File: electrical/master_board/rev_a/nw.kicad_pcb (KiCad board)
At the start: 2 copper layers, 0 parts

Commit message: Inject the PCB outlines into master/center/ne/nw/se/sw PCB's.
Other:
- board outline added: 42.2 x 39 mm
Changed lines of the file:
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@@
     (uvia_drill 0.1)
   )
+  (gr_line (start 70.00 61.00) (end 70.00 26.46) (layer Edge.Cuts) (width 0.05))
+  (gr_line (start 70.00 26.46) (end 69.99 26.33) (layer Edge.Cuts) (width 0.05))
+  (gr_line (start 69.99 26.33) (end 69.98 26.19) (layer Edge.Cuts) (width 0.05))
+  (gr_line (start 69.98 26.19) (end 69.95 26.06) (layer Edge.Cuts) (width 0.05))
+  (gr_line (start 69.95 26.06) (end 69.90 25.94) (layer Edge.Cuts) (width 0.05))
+  (gr_line (start 69.90 25.94) (end 69.85 25.81) (layer Edge.Cuts) (width 0.05))
+  (gr_line (start 69.85 25.81) (end 69.79 25.69) (layer Edge.Cuts) (width 0.05))
+  (gr_line (start 69.79 25.69) (end 69.71 25.58) (layer Edge.Cuts) (width 0.05))
+  (gr_line (start 69.71 25.58) (end 69.63 25.48) (layer Edge.Cuts) (width 0.05))
+  (gr_line (start 69.63 25.48) (end 69.54 25.38) (layer Edge.Cuts) (width 0.05))
+  (gr_line (start 69.54 25.38) (end 69.43 25.29) (layer Edge.Cuts) (width 0.05))
+  (gr_line (start 69.43 25.29) (end 69.33 25.21) (layer Edge.Cuts) (width 0.05))
+  (gr_line (start 69.33 25.21) (end 69.21 25.14) (layer Edge.Cuts) (width 0.05))
+  (gr_line (start 69.21 25.14) (end 69.09 25.08) (layer Edge.Cuts) (width 0.05))
+  (gr_line (start 69.09 25.08) (end 68.96 25.04) (layer Edge.Cuts) (width 0.05))
+  (gr_line (start 68.96 25.04) (end 68.83 25.00) (layer Edge.Cuts) (width 0.05))
+  (gr_line (start 68.83 25.00) (end 68.70 24.98) (layer Edge.Cuts) (width 0.05))
+  (gr_line (start 68.70 24.98) (end 68.57 24.96) (layer Edge.Cuts) (width 0.05))
+  (gr_line (start 68.57 24.96) (end 68.43 24.96) (layer Edge.Cuts) (width 0.05))
+  (gr_line (start 68.43 24.96) (end 68.30 24.98) (layer Edge.Cuts) (width 0.05))
+  (gr_line (start 68.30 24.98) (end 68.17 25.00) (layer Edge.Cuts) (width 0.05))
+  (gr_line (start 68.17 25.00) (end 68.04 25.04) (layer Edge.Cuts) (width 0.05))
+  (gr_line (start 68.04 25.04) (end 67.91 25.08) (layer Edge.Cuts) (width 0.05))
+  (gr_line (start 67.91 25.08) (end 67.91 25.08) (layer Edge.Cuts) (width 0.05))
+  (gr_line (start 67.91 25.08) (end 60.81 28.54) (layer Edge.Cuts) (width 0.05))
+  (gr_line (start 60.81 28.54) (end 54.08 32.67) (layer Edge.Cuts) (width 0.05))
+  (gr_line (start 54.08 32.67) (end 47.79 37.42) (layer Edge.Cuts) (width 0.05))
+  (gr_line (start 47.79 37.42) (end 41.98 42.77) (layer Edge.Cuts) (width 0.05))
+  (gr_line (start 41.98 42.77) (end 36.71 48.65) (layer Edge.Cuts) (width 0.05))
+  (gr_line (start 36.71 48.65) (end 32.04 55.01) (layer Edge.Cuts) (width 0.05))
+  (gr_line (start 32.04 55.01) (end 28.01 61.80) (layer Edge.Cuts) (width 0.05))
+  (gr_line (start 28.01 61.80) (end 27.95 61.92) (layer Edge.Cuts) (width 0.05))
+  (gr_line (start 27.95 61.92) (end 27.90 62.04) (layer Edge.Cuts) (width 0.05))
+  (gr_line (start 27.90 62.04) (end 27.87 62.17) (layer Edge.Cuts) (width 0.05))
+  (gr_line (start 27.87 62.17) (end 27.85 62.31) (layer Edge.Cuts) (width 0.05))
+  (gr_line (start 27.85 62.31) (end 27.83 62.44) (layer Edge.Cuts) (width 0.05))
+  (gr_line (start 27.83 62.44) (end 27.84 62.57) (layer Edge.Cuts) (width 0.05))
+  (gr_line (start 27.84 62.57) (end 27.85 62.71) (layer Edge.Cuts) (width 0.05))
+  (gr_line (start 27.85 62.71) (end 27.87 62.84) (layer Edge.Cuts) (width 0.05))
+  (gr_line (start 27.87 62.84) (end 27.91 62.97) (layer Edge.Cuts) (width 0.05))
+  (gr_line (start 27.91 62.97) (end 27.96 63.09) (layer Edge.Cuts) (width 0.05))
+  (gr_line (start 27.96 63.09) (end 28.01 63.21) (layer Edge.Cuts) (width 0.05))
+  (gr_line (start 28.01 63.21) (end 28.08 63.33) (layer Edge.Cuts) (width 0.05))
+  (gr_line (start 28.08 63.33) (end 28.16 63.44) (layer Edge.Cuts) (width 0.05))
+  (gr_line (start 28.16 63.44) (end 28.25 63.54) (layer Edge.Cuts) (width 0.05))
+  (gr_line (start 28.25 63.54) (end 28.35 63.63) (layer Edge.Cuts) (width 0.05))
+  (gr_line (start 28.35 63.63) (end 28.45 63.72) (layer Edge.Cuts) (width 0.05))
+  (gr_line (start 28.45 63.72) (end 28.57 63.79) (layer Edge.Cuts) (width 0.05))
+  (gr_line (start 28.57 63.79) (end 28.68 63.85) (layer Edge.Cuts) (width 0.05))
+  (gr_line (start 28.68 63.85) (end 28.81 63.90) (layer Edge.Cuts) (width 0.05))
+  (gr_line (start 28.81 63.90) (end 28.94 63.95) (layer Edge.Cuts) (width 0.05))
+  (gr_line (start 28.94 63.95) (end 29.07 63.98) (layer Edge.Cuts) (width 0.05))
+  (gr_line (start 29.07 63.98) (end 29.20 63.99) (layer Edge.Cuts) (width 0.05))
+  (gr_line (start 29.20 63.99) (end 29.33 64.00) (layer Edge.Cuts) (width 0.05))
+  (gr_line (start 29.33 64.00) (end 37.50 64.00) (layer Edge.Cuts) (width 0.05))
+  (gr_line (start 37.50 64.00) (end 37.50 62.50) (layer Edge.Cuts) (width 0.05))
+  (gr_line (start 37.50 62.50) (end 37.51 62.37) (layer Edge.Cuts) (width 0.05))
+  (gr_line (start 37.51 62.37) (end 37.52 62.24) (layer Edge.Cuts) (width 0.05))
+  (gr_line (start 37.52 62.24) (end 37.55 62.11) (layer Edge.Cuts) (width 0.05))
+  (gr_line (start 37.55 62.11) (end 37.59 61.99) (layer Edge.Cuts) (width 0.05))
+  (gr_line (start 37.59 61.99) (end 37.64 61.87) (layer Edge.Cuts) (width 0.05))
+  (gr_line (start 37.64 61.87) (end 37.70 61.75) (layer Edge.Cuts) (width 0.05))
+  (gr_line (start 37.70 61.75) (end 37.77 61.64) (layer Edge.Cuts) (width 0.05))
+  (gr_line (start 37.77 61.64) (end 37.85 61.54) (layer Edge.Cuts) (width 0.05))
+  (gr_line (start 37.85 61.54) (end 37.94 61.44) (layer Edge.Cuts) (width 0.05))
+  (gr_line (start 37.94 61.44) (end 38.04 61.35) (layer Edge.Cuts) (width 0.05))
+  (gr_line (start 38.04 61.35) (end 38.14 61.27) (layer Edge.Cuts) (width 0.05))
+  (gr_line (start 38.14 61.27) (end 38.25 61.20) (layer Edge.Cuts) (width 0.05))
+  (gr_line (start 38.25 61.20) (end 38.37 61.14) (layer Edge.Cuts) (width 0.05))
+  (gr_line (start 38.37 61.14) (end 38.49 61.09) (layer Edge.Cuts) (width 0.05))
+  (gr_line (start 38.49 61.09) (end 38.61 61.05) (layer Edge.Cuts) (width 0.05))
+  (gr_line (start 38.61 61.05) (end 38.74 61.02) (layer Edge.Cuts) (width 0.05))
+  (gr_line (start 38.74 61.02) (end 38.87 61.01) (layer Edge.Cuts) (width 0.05))
+  (gr_line (start 38.87 61.01) (end 39.00 61.00) (layer Edge.Cuts) (width 0.05))
+  (gr_line (start 39.00 61.00) (end 70.00 61.00) (layer Edge.Cuts) (width 0.05))
 )

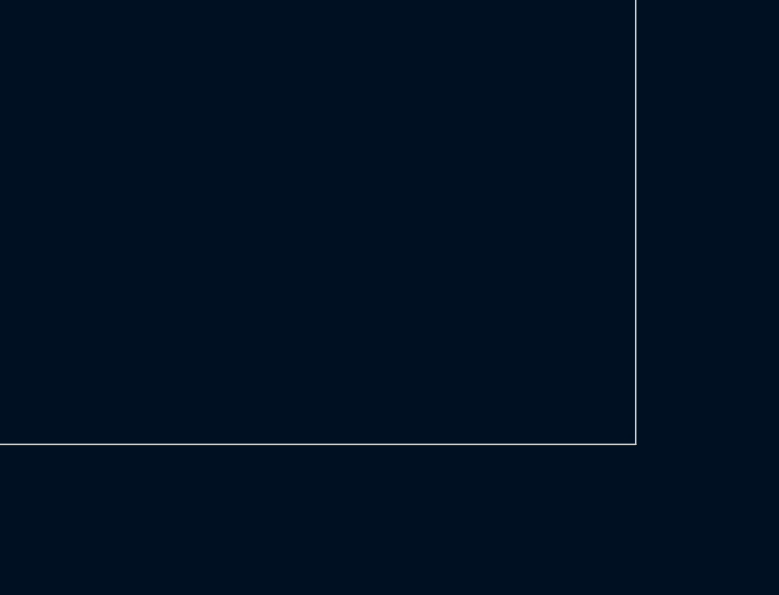
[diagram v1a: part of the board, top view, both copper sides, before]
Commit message: Updated some of the schematics and PCB's via hr2_models.py .
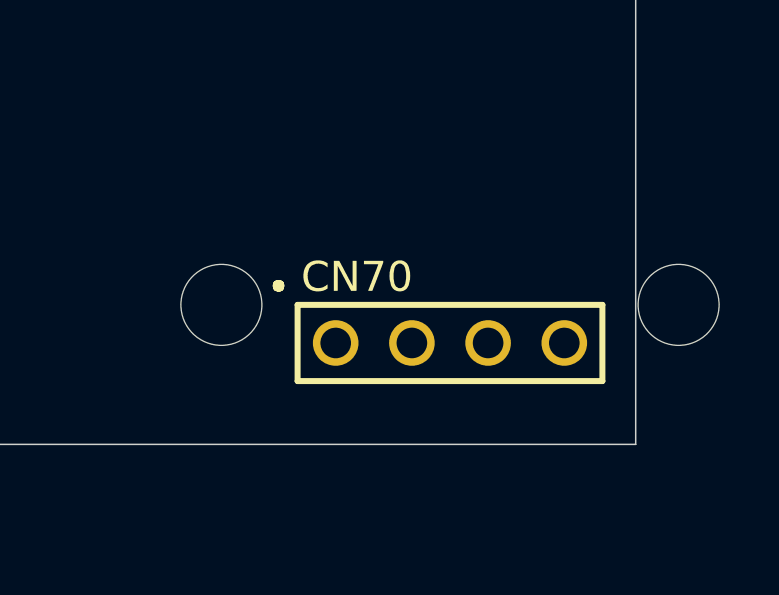
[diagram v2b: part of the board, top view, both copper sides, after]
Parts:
- added CN70: HCSR04H;F1X4, HR2:HCSR04_F1x4H_MATE, F.Cu at (63.8, 57.6)
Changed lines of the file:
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@@
   (general
     (thickness 1.6)
-    (drawings 0)
+    (drawings 75)
     (tracks 0)
     (zones 0)
-    (modules 0)
+    (modules 1)
     (nets 1)
   )
@@
     (47 F.CrtYd user)
     (48 B.Fab user)
-    (49 F.Fab user)
+    (49 F.Fab user hide)
   )
   (setup
@@
     (uvia_dia 0.3)
     (uvia_drill 0.1)
+    (add_net "Net-(CN70-Pad1)")
+    (add_net "Net-(CN70-Pad2)")
+    (add_net "Net-(CN70-Pad3)")
+    (add_net "Net-(CN70-Pad4)")
+  )
+  (module HR2:HCSR04_F1x4H_MATE (layer F.Cu)
+    (at 63.81 57.62)
+    (fp_text reference CN70 (at -3.1 -2.2) (layer F.SilkS)
+      (effects (font (size 1 1) (thickness 0.2)))
+    )
+    (fp_text value HCSR04H;F1X4 (at 0 -2) (layer F.Fab)
+      (effects (font (size 1 1) (thickness 0.2)))
+    )
+    (fp_line (start 5.08 -1.27) (end 5.08 1.27) (layer F.SilkS) (width 0.2))
+    (fp_line (start 5.08 1.27) (end -5.08 1.27) (layer F.SilkS) (width 0.2))
+    (fp_line (start -5.08 1.27) (end -5.08 -1.27) (layer F.SilkS) (width 0.2))
+    (fp_line (start -5.08 -1.27) (end 5.08 -1.27) (layer F.SilkS) (width 0.2))
+    (fp_line (start -5.62 -1.91) (end -5.64 -1.98) (layer F.SilkS) (width 0.2))
+    (fp_line (start -5.64 -1.98) (end -5.71 -2) (layer F.SilkS) (width 0.2))
+    (fp_line (start -5.71 -2) (end -5.79 -1.98) (layer F.SilkS) (width 0.2))
+    (fp_line (start -5.79 -1.98) (end -5.81 -1.91) (layer F.SilkS) (width 0.2))
+    (fp_line (start -5.81 -1.91) (end -5.79 -1.83) (layer F.SilkS) (width 0.2))
+    (fp_line (start -5.79 -1.83) (end -5.71 -1.8) (layer F.SilkS) (width 0.2))
+    (fp_line (start -5.71 -1.8) (end -5.64 -1.83) (layer F.SilkS) (width 0.2))
+    (fp_line (start -5.64 -1.83) (end -5.62 -1.91) (layer F.SilkS) (width 0.2))
+    (pad "HCSR04 West Tie Down Hole" np_thru_hole circle (at -7.62 -1.27) (size 2.7 2.7) (drill 2.7) (layers *.Cu *.Mask))
+    (pad "HCSR04 East Tie Down Hole" np_thru_hole circle (at 7.62 -1.27) (size 2.7 2.7) (drill 2.7) (layers *.Cu *.Mask))
+    (pad 4 thru_hole circle (at 3.81 0) (size 1.52 1.52) (drill 1.02) (layers *.Cu *.Mask))
+    (pad 3 thru_hole circle (at 1.27 0) (size 1.52 1.52) (drill 1.02) (layers *.Cu *.Mask))
+    (pad 2 thru_hole circle (at -1.27 0) (size 1.52 1.52) (drill 1.02) (layers *.Cu *.Mask))
+    (pad 1 thru_hole circle (at -3.81 0) (size 1.52 1.52) (drill 1.02) (layers *.Cu *.Mask))
   )
   (gr_line (start 70.00 61.00) (end 70.00 26.46) (layer Edge.Cuts) (width 0.05))

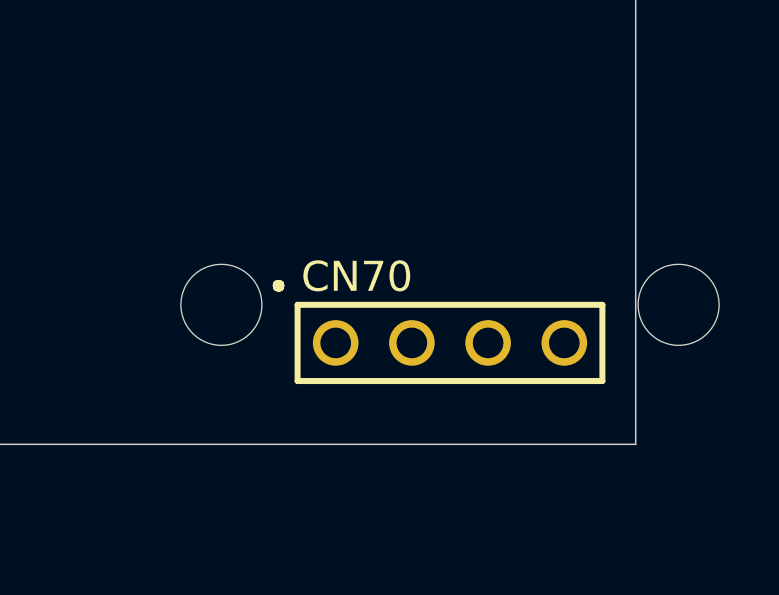
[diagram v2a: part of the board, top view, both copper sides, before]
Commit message: Successfully placed a font surface non-rotated footprint in ne.kicad_pcb.
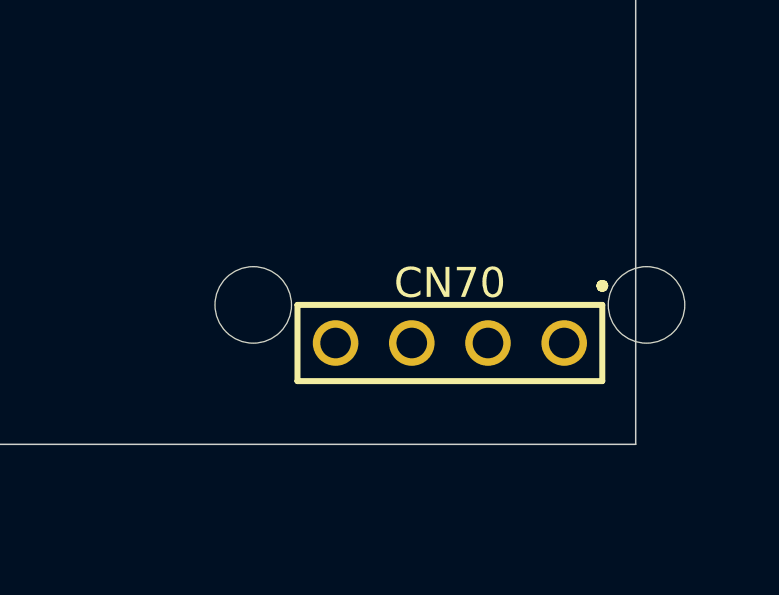
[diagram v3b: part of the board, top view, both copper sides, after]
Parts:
- CN70: value HCSR04H;F1X4 -> HCSR04;F1x4H; footprint HR2:HCSR04_F1x4H_MATE -> HR2:HCSR04_F1x4H
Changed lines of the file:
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@@
     (add_net "Net-(CN70-Pad4)")
   )
-  (module HR2:HCSR04_F1x4H_MATE (layer F.Cu)
-    (at 63.81 57.62)
-    (fp_text reference CN70 (at -3.1 -2.2) (layer F.SilkS)
+  (module HR2:HCSR04_F1x4H (layer F.Cu)
+    (at 63.8063 57.6226)
+    (fp_text reference CN70 (at 0 -2) (layer F.SilkS)
       (effects (font (size 1 1) (thickness 0.2)))
     )
-    (fp_text value HCSR04H;F1X4 (at 0 -2) (layer F.Fab)
+    (fp_text value HCSR04;F1x4H (at 0 0) (layer F.Fab)
       (effects (font (size 1 1) (thickness 0.2)))
     )
@@
     (fp_line (start -5.08 1.27) (end -5.08 -1.27) (layer F.SilkS) (width 0.2))
     (fp_line (start -5.08 -1.27) (end 5.08 -1.27) (layer F.SilkS) (width 0.2))
-    (fp_line (start -5.62 -1.91) (end -5.64 -1.98) (layer F.SilkS) (width 0.2))
-    (fp_line (start -5.64 -1.98) (end -5.71 -2) (layer F.SilkS) (width 0.2))
-    (fp_line (start -5.71 -2) (end -5.79 -1.98) (layer F.SilkS) (width 0.2))
-    (fp_line (start -5.79 -1.98) (end -5.81 -1.91) (layer F.SilkS) (width 0.2))
-    (fp_line (start -5.81 -1.91) (end -5.79 -1.83) (layer F.SilkS) (width 0.2))
-    (fp_line (start -5.79 -1.83) (end -5.71 -1.8) (layer F.SilkS) (width 0.2))
-    (fp_line (start -5.71 -1.8) (end -5.64 -1.83) (layer F.SilkS) (width 0.2))
-    (fp_line (start -5.64 -1.83) (end -5.62 -1.91) (layer F.SilkS) (width 0.2))
-    (pad "HCSR04 West Tie Down Hole" np_thru_hole circle (at -7.62 -1.27) (size 2.7 2.7) (drill 2.7) (layers *.Cu *.Mask))
-    (pad "HCSR04 East Tie Down Hole" np_thru_hole circle (at 7.62 -1.27) (size 2.7 2.7) (drill 2.7) (layers *.Cu *.Mask))
-    (pad 4 thru_hole circle (at 3.81 0) (size 1.52 1.52) (drill 1.02) (layers *.Cu *.Mask))
-    (pad 3 thru_hole circle (at 1.27 0) (size 1.52 1.52) (drill 1.02) (layers *.Cu *.Mask))
-    (pad 2 thru_hole circle (at -1.27 0) (size 1.52 1.52) (drill 1.02) (layers *.Cu *.Mask))
-    (pad 1 thru_hole circle (at -3.81 0) (size 1.52 1.52) (drill 1.02) (layers *.Cu *.Mask))
+    (fp_line (start 5.18 -1.91) (end 5.15 -1.98) (layer F.SilkS) (width 0.2))
+    (fp_line (start 5.15 -1.98) (end 5.08 -2) (layer F.SilkS) (width 0.2))
+    (fp_line (start 5.08 -2) (end 5.01 -1.98) (layer F.SilkS) (width 0.2))
+    (fp_line (start 5.01 -1.98) (end 4.98 -1.91) (layer F.SilkS) (width 0.2))
+    (fp_line (start 4.98 -1.91) (end 5.01 -1.83) (layer F.SilkS) (width 0.2))
+    (fp_line (start 5.01 -1.83) (end 5.08 -1.8) (layer F.SilkS) (width 0.2))
+    (fp_line (start 5.08 -1.8) (end 5.15 -1.83) (layer F.SilkS) (width 0.2))
+    (fp_line (start 5.15 -1.83) (end 5.18 -1.91) (layer F.SilkS) (width 0.2))
+    (pad "HCSR04 West Tie Down Hole" np_thru_hole circle (at -6.555 -1.27) (size 2.55 2.55) (drill 2.55) (layers *.Cu *.Mask))
+    (pad "HCSR04 East Tie Down Hole" np_thru_hole circle (at 6.555 -1.27) (size 2.55 2.55) (drill 2.55) (layers *.Cu *.Mask))
+    (pad 4 thru_hole circle (at -3.81 0) (size 1.52 1.52) (drill 1.02) (layers *.Cu *.Mask))
+    (pad 3 thru_hole circle (at -1.27 0) (size 1.52 1.52) (drill 1.02) (layers *.Cu *.Mask))
+    (pad 2 thru_hole circle (at 1.27 0) (size 1.52 1.52) (drill 1.02) (layers *.Cu *.Mask))
+    (pad 1 thru_hole circle (at 3.81 0) (size 1.52 1.52) (drill 1.02) (layers *.Cu *.Mask))
   )
-  (gr_line (start 70.00 61.00) (end 70.00 26.46) (layer Edge.Cuts) (width 0.05))
-  (gr_line (start 70.00 26.46) (end 69.99 26.33) (layer Edge.Cuts) (width 0.05))
+  (gr_line (start 70 61) (end 70 26.46) (layer Edge.Cuts) (width 0.05))
+  (gr_line (start 70 26.46) (end 69.99 26.33) (layer Edge.Cuts) (width 0.05))
   (gr_line (start 69.99 26.33) (end 69.98 26.19) (layer Edge.Cuts) (width 0.05))
   (gr_line (start 69.98 26.19) (end 69.95 26.06) (layer Edge.Cuts) (width 0.05))
-  (gr_line (start 69.95 26.06) (end 69.90 25.94) (layer Edge.Cuts) (width 0.05))
-  (gr_line (start 69.90 25.94) (end 69.85 25.81) (layer Edge.Cuts) (width 0.05))
+  (gr_line (start 69.95 26.06) (end 69.9 25.94) (layer Edge.Cuts) (width 0.05))
+  (gr_line (start 69.9 25.94) (end 69.85 25.81) (layer Edge.Cuts) (width 0.05))
   (gr_line (start 69.85 25.81) (end 69.79 25.69) (layer Edge.Cuts) (width 0.05))
   (gr_line (start 69.79 25.69) (end 69.71 25.58) (layer Edge.Cuts) (width 0.05))
@@
   (gr_line (start 69.21 25.14) (end 69.09 25.08) (layer Edge.Cuts) (width 0.05))
   (gr_line (start 69.09 25.08) (end 68.96 25.04) (layer Edge.Cuts) (width 0.05))
-  (gr_line (start 68.96 25.04) (end 68.83 25.00) (layer Edge.Cuts) (width 0.05))
-  (gr_line (start 68.83 25.00) (end 68.70 24.98) (layer Edge.Cuts) (width 0.05))
-  (gr_line (start 68.70 24.98) (end 68.57 24.96) (layer Edge.Cuts) (width 0.05))
+  (gr_line (start 68.96 25.04) (end 68.83 25) (layer Edge.Cuts) (width 0.05))
+  (gr_line (start 68.83 25) (end 68.7 24.98) (layer Edge.Cuts) (width 0.05))
+  (gr_line (start 68.7 24.98) (end 68.57 24.96) (layer Edge.Cuts) (width 0.05))
   (gr_line (start 68.57 24.96) (end 68.43 24.96) (layer Edge.Cuts) (width 0.05))
-  (gr_line (start 68.43 24.96) (end 68.30 24.98) (layer Edge.Cuts) (width 0.05))
-  (gr_line (start 68.30 24.98) (end 68.17 25.00) (layer Edge.Cuts) (width 0.05))
-  (gr_line (start 68.17 25.00) (end 68.04 25.04) (layer Edge.Cuts) (width 0.05))
+  (gr_line (start 68.43 24.96) (end 68.3 24.98) (layer Edge.Cuts) (width 0.05))
+  (gr_line (start 68.3 24.98) (end 68.17 25) (layer Edge.Cuts) (width 0.05))
+  (gr_line (start 68.17 25) (end 68.04 25.04) (layer Edge.Cuts) (width 0.05))
   (gr_line (start 68.04 25.04) (end 67.91 25.08) (layer Edge.Cuts) (width 0.05))
   (gr_line (start 67.91 25.08) (end 67.91 25.08) (layer Edge.Cuts) (width 0.05))
@@
   (gr_line (start 41.98 42.77) (end 36.71 48.65) (layer Edge.Cuts) (width 0.05))
   (gr_line (start 36.71 48.65) (end 32.04 55.01) (layer Edge.Cuts) (width 0.05))
-  (gr_line (start 32.04 55.01) (end 28.01 61.80) (layer Edge.Cuts) (width 0.05))
-  (gr_line (start 28.01 61.80) (end 27.95 61.92) (layer Edge.Cuts) (width 0.05))
-  (gr_line (start 27.95 61.92) (end 27.90 62.04) (layer Edge.Cuts) (width 0.05))
-  (gr_line (start 27.90 62.04) (end 27.87 62.17) (layer Edge.Cuts) (width 0.05))
+  (gr_line (start 32.04 55.01) (end 28.01 61.8) (layer Edge.Cuts) (width 0.05))
+  (gr_line (start 28.01 61.8) (end 27.95 61.92) (layer Edge.Cuts) (width 0.05))
+  (gr_line (start 27.95 61.92) (end 27.9 62.04) (layer Edge.Cuts) (width 0.05))
+  (gr_line (start 27.9 62.04) (end 27.87 62.17) (layer Edge.Cuts) (width 0.05))
   (gr_line (start 27.87 62.17) (end 27.85 62.31) (layer Edge.Cuts) (width 0.05))
   (gr_line (start 27.85 62.31) (end 27.83 62.44) (layer Edge.Cuts) (width 0.05))
@@
   (gr_line (start 28.45 63.72) (end 28.57 63.79) (layer Edge.Cuts) (width 0.05))
   (gr_line (start 28.57 63.79) (end 28.68 63.85) (layer Edge.Cuts) (width 0.05))
-  (gr_line (start 28.68 63.85) (end 28.81 63.90) (layer Edge.Cuts) (width 0.05))
-  (gr_line (start 28.81 63.90) (end 28.94 63.95) (layer Edge.Cuts) (width 0.05))
+  (gr_line (start 28.68 63.85) (end 28.81 63.9) (layer Edge.Cuts) (width 0.05))
+  (gr_line (start 28.81 63.9) (end 28.94 63.95) (layer Edge.Cuts) (width 0.05))
   (gr_line (start 28.94 63.95) (end 29.07 63.98) (layer Edge.Cuts) (width 0.05))
-  (gr_line (start 29.07 63.98) (end 29.20 63.99) (layer Edge.Cuts) (width 0.05))
-  (gr_line (start 29.20 63.99) (end 29.33 64.00) (layer Edge.Cuts) (width 0.05))
-  (gr_line (start 29.33 64.00) (end 37.50 64.00) (layer Edge.Cuts) (width 0.05))
-  (gr_line (start 37.50 64.00) (end 37.50 62.50) (layer Edge.Cuts) (width 0.05))
-  (gr_line (start 37.50 62.50) (end 37.51 62.37) (layer Edge.Cuts) (width 0.05))
+  (gr_line (start 29.07 63.98) (end 29.2 63.99) (layer Edge.Cuts) (width 0.05))
+  (gr_line (start 29.2 63.99) (end 29.33 64) (layer Edge.Cuts) (width 0.05))
+  (gr_line (start 29.33 64) (end 37.5 64) (layer Edge.Cuts) (width 0.05))
+  (gr_line (start 37.5 64) (end 37.5 62.5) (layer Edge.Cuts) (width 0.05))
+  (gr_line (start 37.5 62.5) (end 37.51 62.37) (layer Edge.Cuts) (width 0.05))
   (gr_line (start 37.51 62.37) (end 37.52 62.24) (layer Edge.Cuts) (width 0.05))
   (gr_line (start 37.52 62.24) (end 37.55 62.11) (layer Edge.Cuts) (width 0.05))
   (gr_line (start 37.55 62.11) (end 37.59 61.99) (layer Edge.Cuts) (width 0.05))
   (gr_line (start 37.59 61.99) (end 37.64 61.87) (layer Edge.Cuts) (width 0.05))
-  (gr_line (start 37.64 61.87) (end 37.70 61.75) (layer Edge.Cuts) (width 0.05))
-  (gr_line (start 37.70 61.75) (end 37.77 61.64) (layer Edge.Cuts) (width 0.05))
+  (gr_line (start 37.64 61.87) (end 37.7 61.75) (layer Edge.Cuts) (width 0.05))
+  (gr_line (start 37.7 61.75) (end 37.77 61.64) (layer Edge.Cuts) (width 0.05))
   (gr_line (start 37.77 61.64) (end 37.85 61.54) (layer Edge.Cuts) (width 0.05))
   (gr_line (start 37.85 61.54) (end 37.94 61.44) (layer Edge.Cuts) (width 0.05))
   (gr_line (start 37.94 61.44) (end 38.04 61.35) (layer Edge.Cuts) (width 0.05))
   (gr_line (start 38.04 61.35) (end 38.14 61.27) (layer Edge.Cuts) (width 0.05))
-  (gr_line (start 38.14 61.27) (end 38.25 61.20) (layer Edge.Cuts) (width 0.05))
-  (gr_line (start 38.25 61.20) (end 38.37 61.14) (layer Edge.Cuts) (width 0.05))
+  (gr_line (start 38.14 61.27) (end 38.25 61.2) (layer Edge.Cuts) (width 0.05))
+  (gr_line (start 38.25 61.2) (end 38.37 61.14) (layer Edge.Cuts) (width 0.05))
   (gr_line (start 38.37 61.14) (end 38.49 61.09) (layer Edge.Cuts) (width 0.05))
   (gr_line (start 38.49 61.09) (end 38.61 61.05) (layer Edge.Cuts) (width 0.05))
   (gr_line (start 38.61 61.05) (end 38.74 61.02) (layer Edge.Cuts) (width 0.05))
   (gr_line (start 38.74 61.02) (end 38.87 61.01) (layer Edge.Cuts) (width 0.05))
-  (gr_line (start 38.87 61.01) (end 39.00 61.00) (layer Edge.Cuts) (width 0.05))
-  (gr_line (start 39.00 61.00) (end 70.00 61.00) (layer Edge.Cuts) (width 0.05))
+  (gr_line (start 38.87 61.01) (end 39 61) (layer Edge.Cuts) (width 0.05))
+  (gr_line (start 39 61) (end 70 61) (layer Edge.Cuts) (width 0.05))
 )
